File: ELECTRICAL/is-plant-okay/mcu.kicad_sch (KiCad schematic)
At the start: 1 part

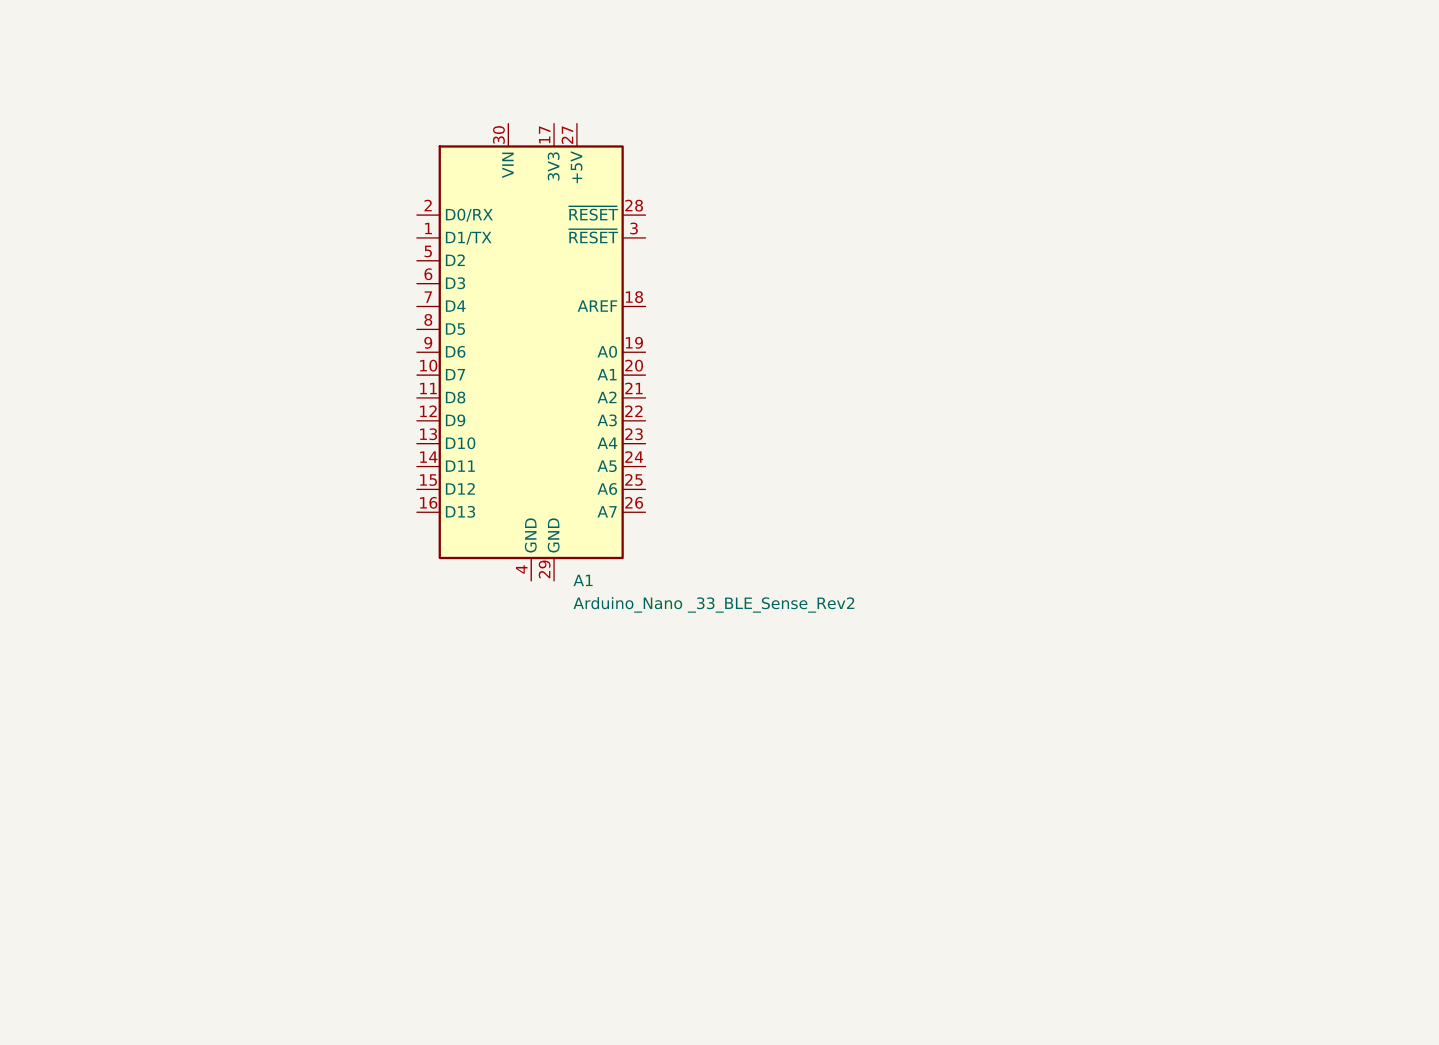
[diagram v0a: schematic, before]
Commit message: add BOM, add changes to MCU
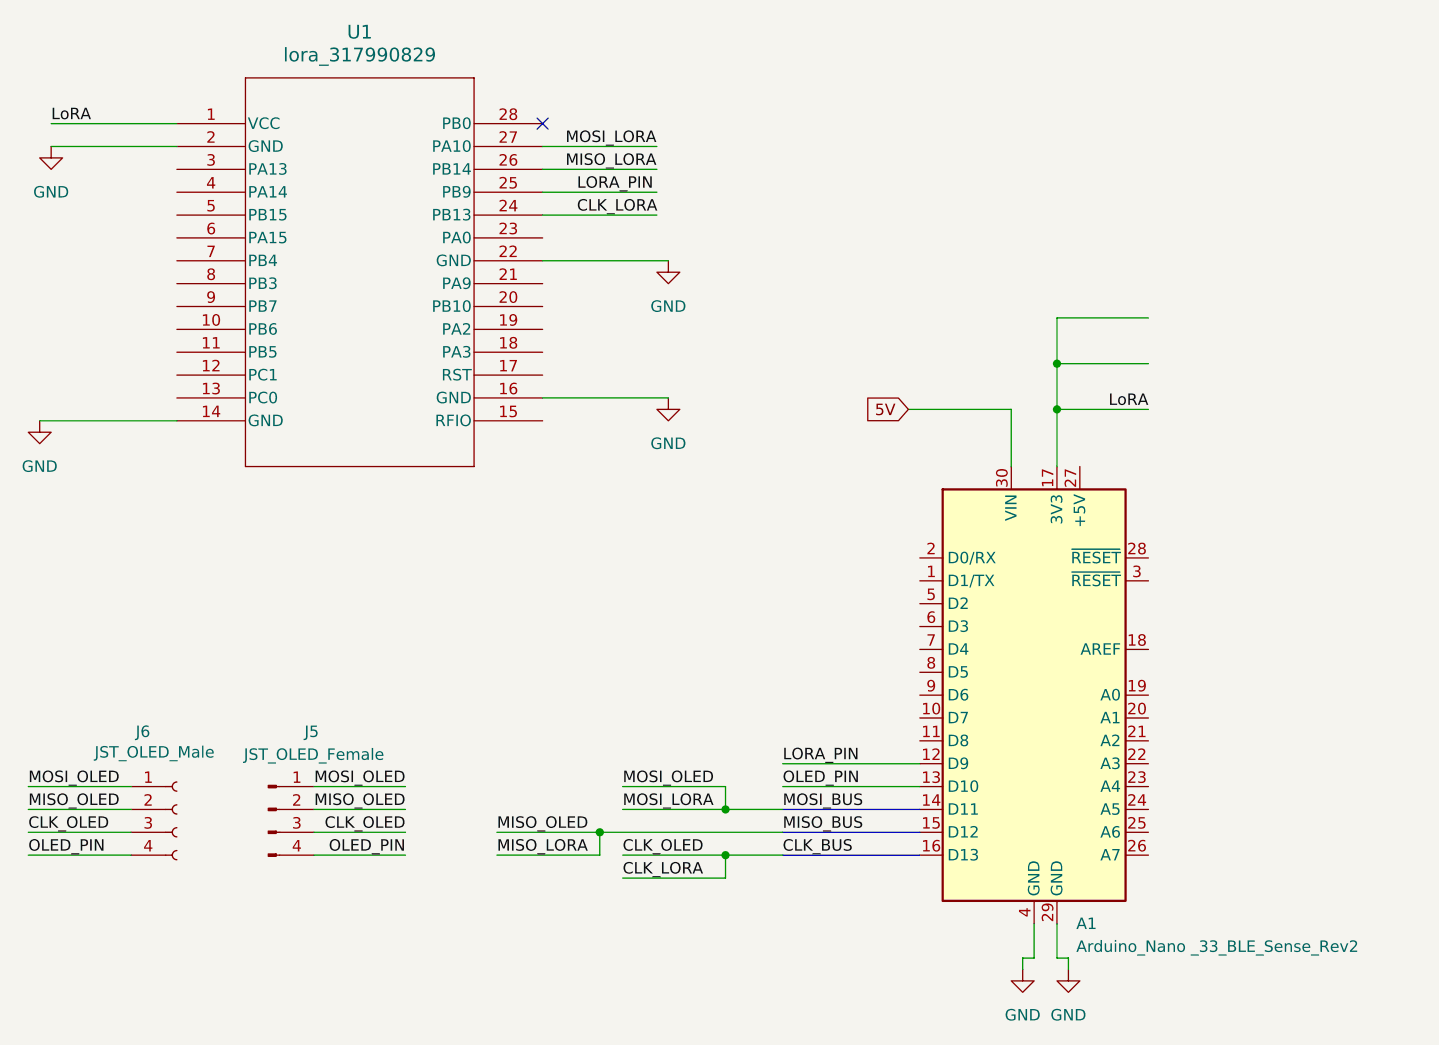
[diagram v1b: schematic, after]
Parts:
- added J5: JST_OLED_Female, symbol Connector:Conn_01x04_Pin
- added J6: JST_OLED_Male, symbol Connector:Conn_01x04_Socket
- added U1: lora_317990829, is-plant-okay-foot:lora_317990829_SEE, symbol is-plant-okay-lib:317990829
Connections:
- net LORA_PIN: now reaches A1.12 (D9)
- net LORA_PIN: now also U1.25 (PB9)
- net OLED_PIN: now reaches A1.13 (D10)
- net OLED_PIN: now also J5.4 (Pin_4), J6.4 (Pin_4)
- net LoRA: now reaches A1.17 (3V3)
- net LoRA: now also U1.1 (VCC)
- net GND: now reaches A1.29 (GND)
- net GND: now also A1.4 (GND), U1.14 (GND), U1.16 (GND), U1.2 (GND), U1.22 (GND)
- net 5V: now reaches A1.30 (VIN)
- new net CLK_BUS: J5.3 (Pin_3), J6.3 (Pin_3), U1.24 (PB13)
- new net MISO_BUS: J5.2 (Pin_2), J6.2 (Pin_2), U1.26 (PB14)
- new net MOSI_BUS: J5.1 (Pin_1), J6.1 (Pin_1), U1.27 (PA10)
- no-connect marks 0 -> 1
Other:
- moved on the sheet: A1

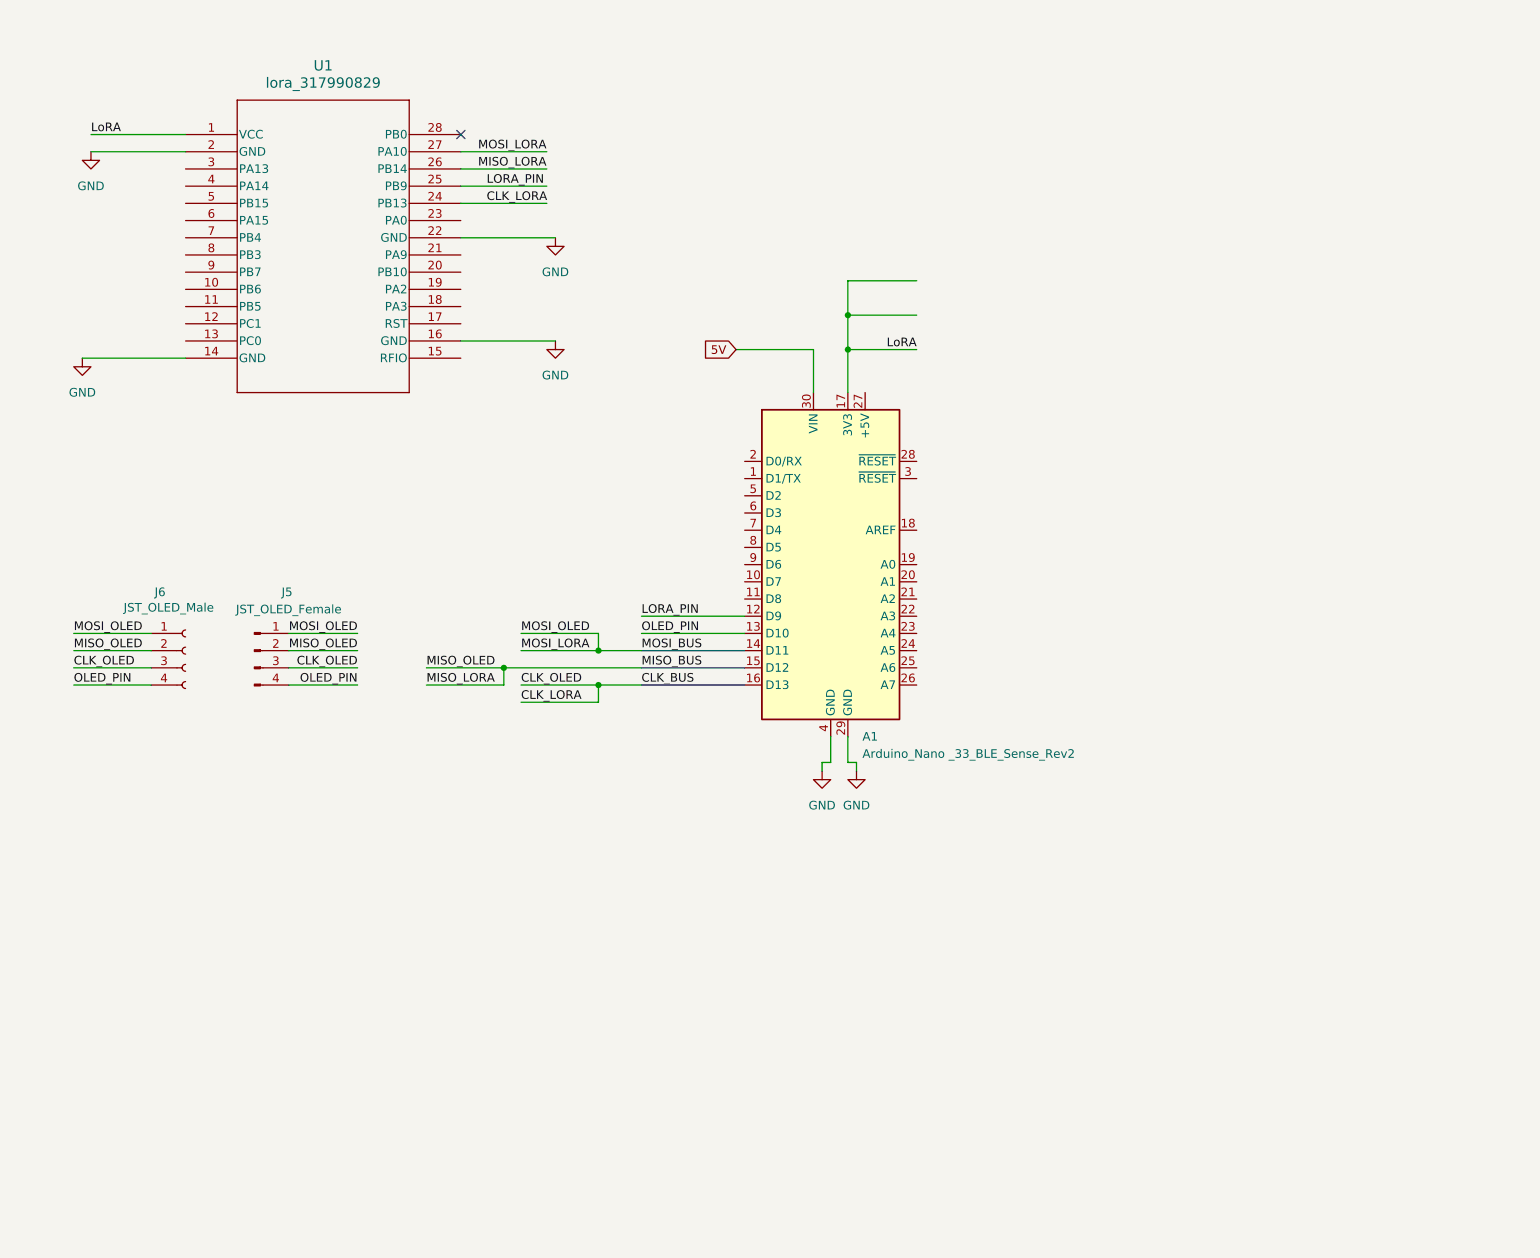
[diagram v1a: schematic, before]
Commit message: changed oled display
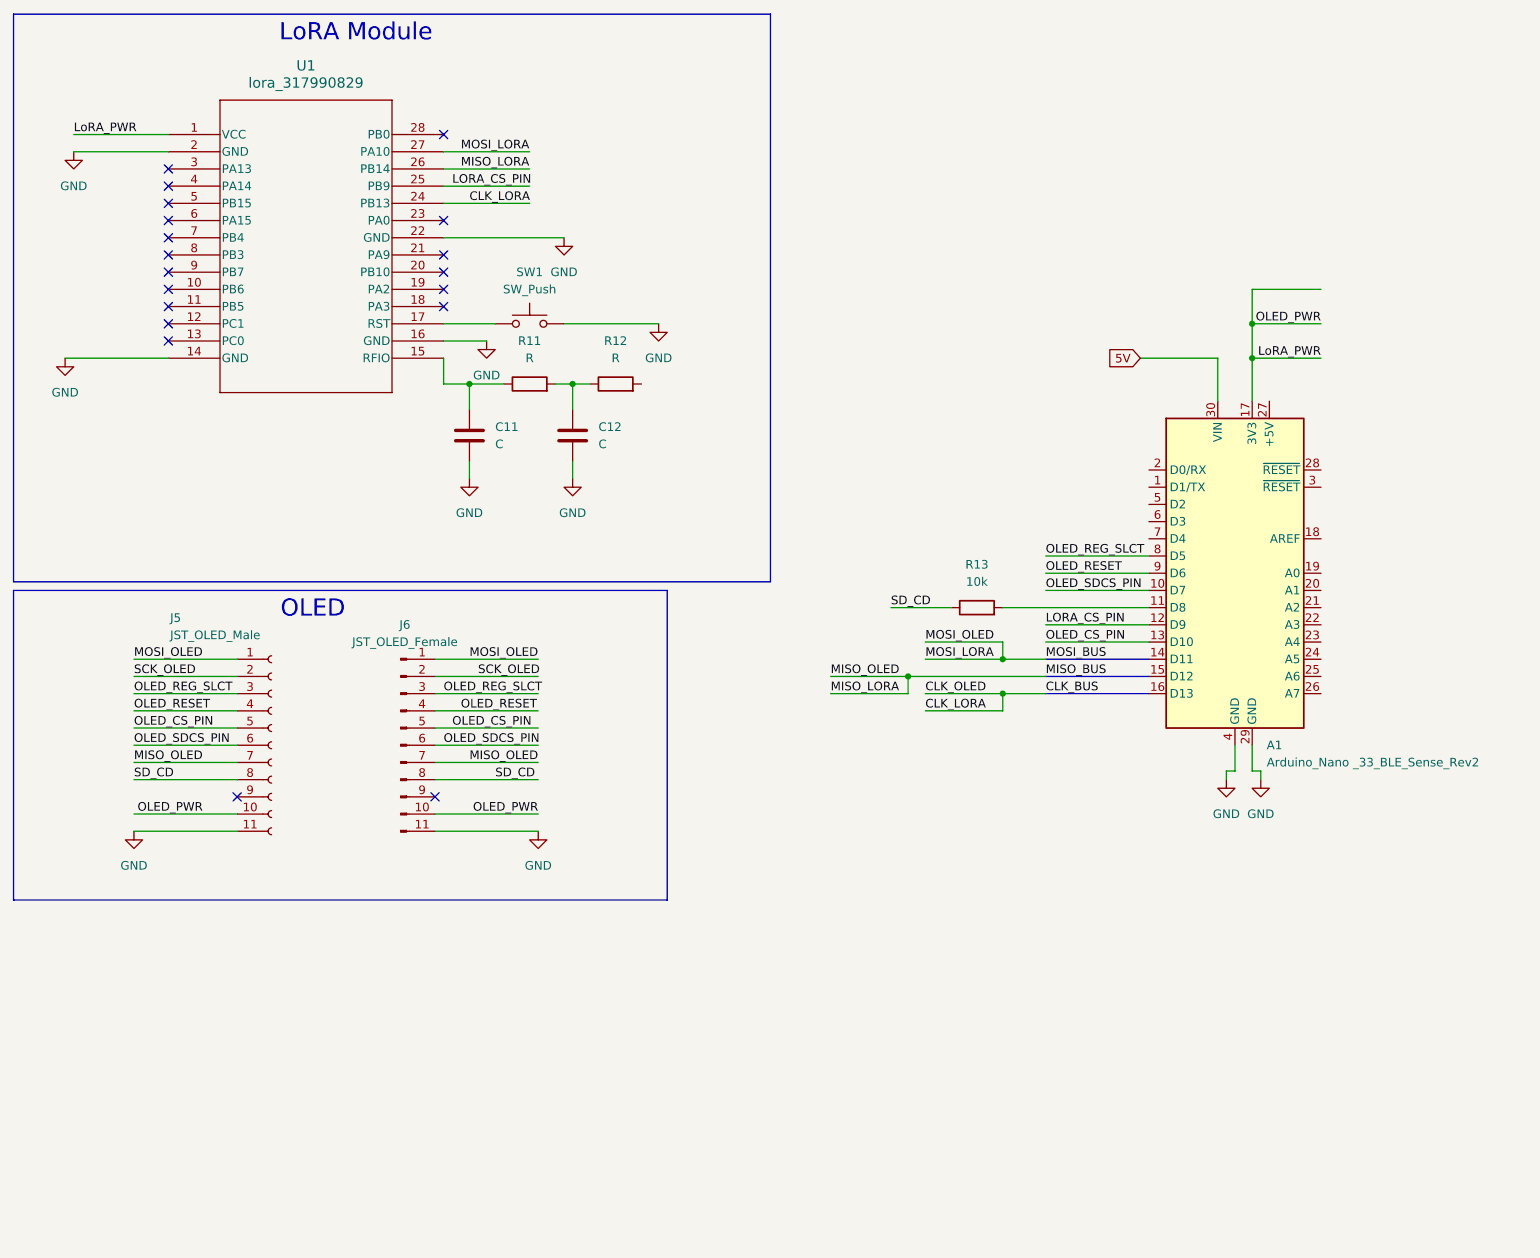
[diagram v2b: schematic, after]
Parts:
- removed J5: JST_OLED_Female, symbol Connector:Conn_01x04_Pin
- removed J6: JST_OLED_Male, symbol Connector:Conn_01x04_Socket
- added C11, C12: C, symbol Device:C
- added J5: JST_OLED_Male, symbol Connector:Conn_01x11_Socket
- added J6: JST_OLED_Female, symbol Connector:Conn_01x11_Pin
- added R11, R12: R, symbol Device:R
- added R13: 10k, symbol Device:R
- added SW1: SW_Push, symbol Switch:SW_Push
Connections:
- net GND: now also C11.2, C12.2, J5.11 (Pin_11), J6.11 (Pin_11), SW1.2
- net MISO_BUS: now also J5.7 (Pin_7), J6.7 (Pin_7)
- net MOSI_BUS: now also J5.1 (Pin_1), J6.1 (Pin_1)
- net at U1.15 (RFIO): now also C11.1, R11.1
- net at U1.17 (RST): now also SW1.1
- net OLED_SDCS_PIN: now reaches A1.10 (D7)
- net OLED_SDCS_PIN: now also J5.6 (Pin_6), J6.6 (Pin_6)
- net at A1.11 (D8): now also R13.2
- net OLED_REG_SLCT: now reaches A1.8 (D5)
- net OLED_REG_SLCT: now also J5.3 (Pin_3), J6.3 (Pin_3)
- net OLED_RESET: now reaches A1.9 (D6)
- net OLED_RESET: now also J5.4 (Pin_4), J6.4 (Pin_4)
- net LORA_PIN renamed LORA_CS_PIN
- net LoRA renamed LoRA_PWR
- net LoRA_PWR: now also J5.10 (Pin_10), J6.10 (Pin_10)
- net OLED_PIN renamed OLED_CS_PIN
- net OLED_CS_PIN: now also J5.5 (Pin_5), J6.5 (Pin_5)
- new net: C12.1, R11.2, R12.1
- new net SCK_OLED: J5.2 (Pin_2), J6.2 (Pin_2)
- new net SD_CD: J5.8 (Pin_8), J6.8 (Pin_8), R13.1
- no-connect marks 1 -> 19
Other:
- note added: "LoRA Module"
- note added: "OLED"
- moved on the sheet: A1, U1

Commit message: feat: added pins for mcu
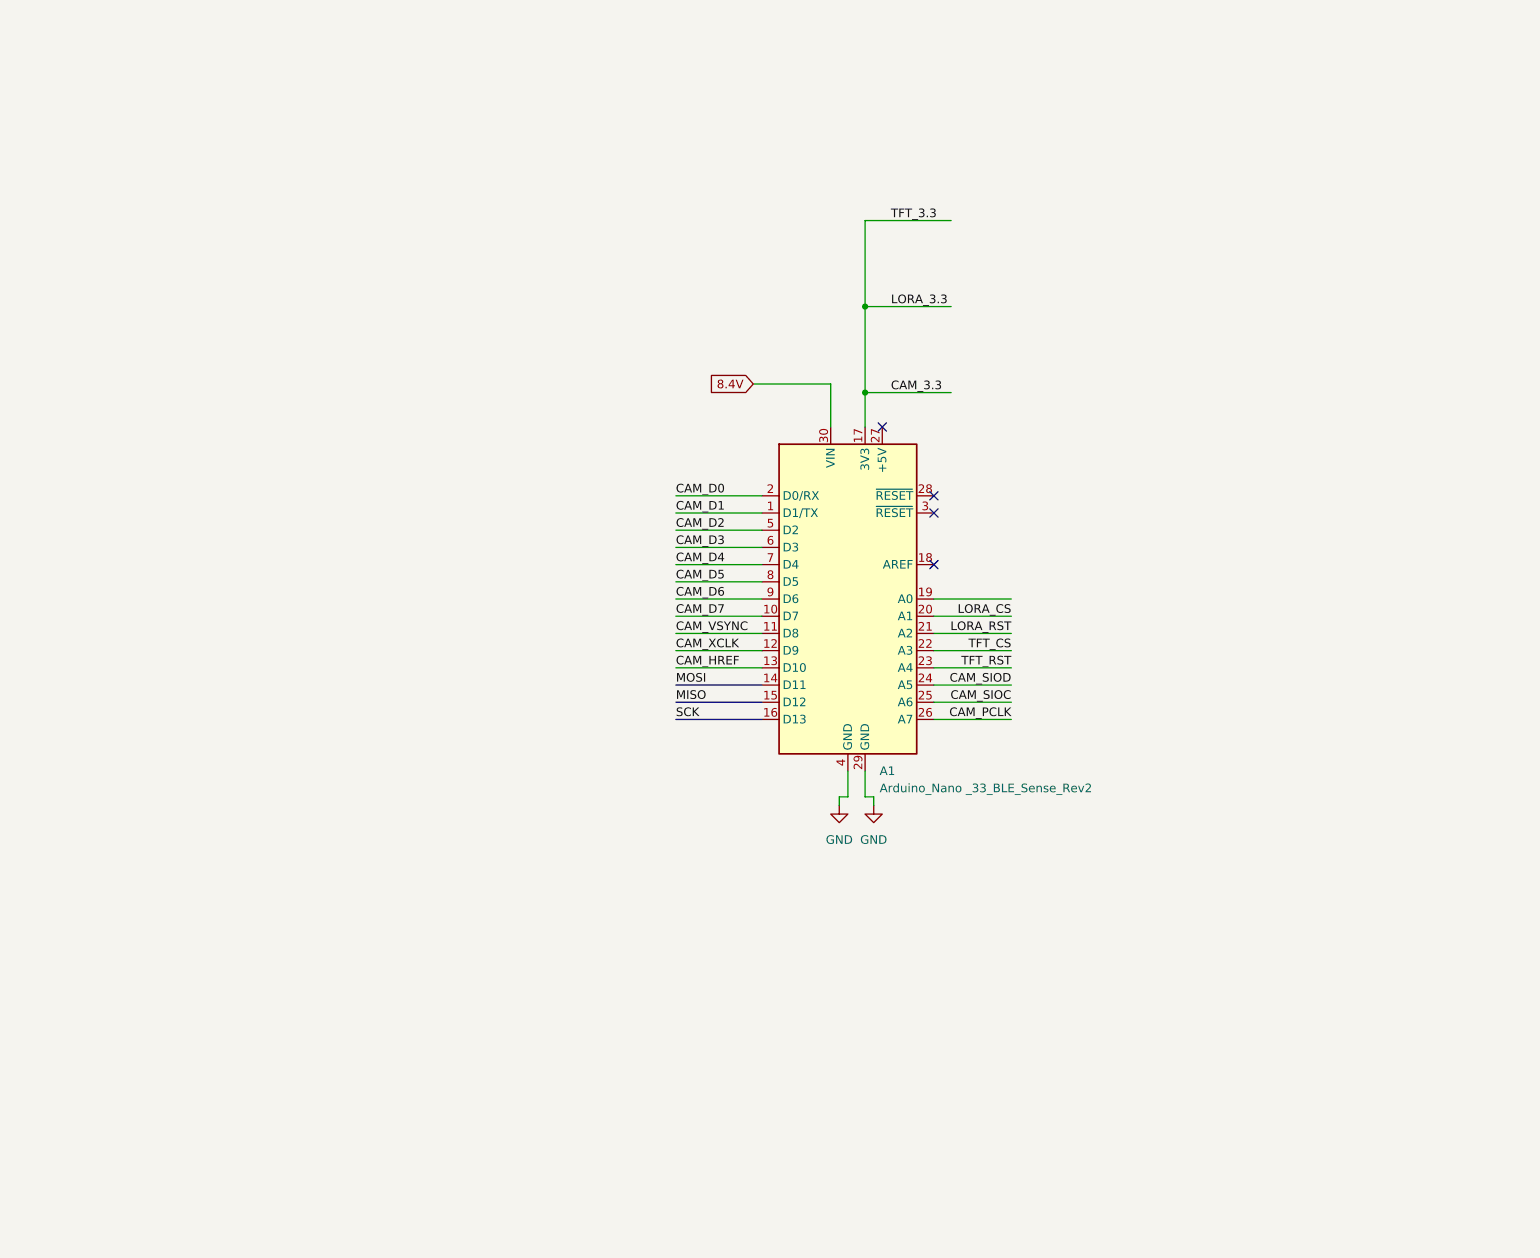
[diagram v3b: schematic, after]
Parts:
- removed C11, C12: C, symbol Device:C
- removed J5: JST_OLED_Male, symbol Connector:Conn_01x11_Socket
- removed J6: JST_OLED_Female, symbol Connector:Conn_01x11_Pin
- removed R11, R12: R, symbol Device:R
- removed R13: 10k, symbol Device:R
- removed SW1: SW_Push, symbol Switch:SW_Push
- removed U1: lora_317990829, is-plant-okay-foot:lora_317990829_SEE, symbol is-plant-okay-lib:317990829
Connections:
- net CAM_VSYNC: now reaches A1.11 (D8)
- net CAM_D1: now reaches A1.1 (D1/TX)
- net CAM_D0: now reaches A1.2 (D0/RX)
- net LORA_CS: now reaches A1.20 (A1)
- net LORA_RST: now reaches A1.21 (A2)
- net TFT_CS: now reaches A1.22 (A3)
- net TFT_RST: now reaches A1.23 (A4)
- net CAM_SIOD: now reaches A1.24 (A5)
- net CAM_SIOC: now reaches A1.25 (A6)
- net CAM_PCLK: now reaches A1.26 (A7)
- net CAM_D2: now reaches A1.5 (D2)
- net CAM_D3: now reaches A1.6 (D3)
- net CAM_D4: now reaches A1.7 (D4)
- net 5V renamed 8.4V
- net LORA_CS_PIN renamed CAM_XCLK
- net LoRA_PWR renamed CAM_3.3
- net OLED_CS_PIN renamed CAM_HREF
- net OLED_REG_SLCT renamed CAM_D5
- net OLED_RESET renamed CAM_D6
- net OLED_SDCS_PIN renamed CAM_D7
- no-connect marks 19 -> 4
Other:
- note removed: "LoRA Module"
- note removed: "OLED"
- moved on the sheet: A1
